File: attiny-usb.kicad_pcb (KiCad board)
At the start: 2 copper layers, 41.6 x 16.4 mm, 13 parts, among them J2 Conn_01x06, J3 Conn_01x02, U1 ATtiny85-20P

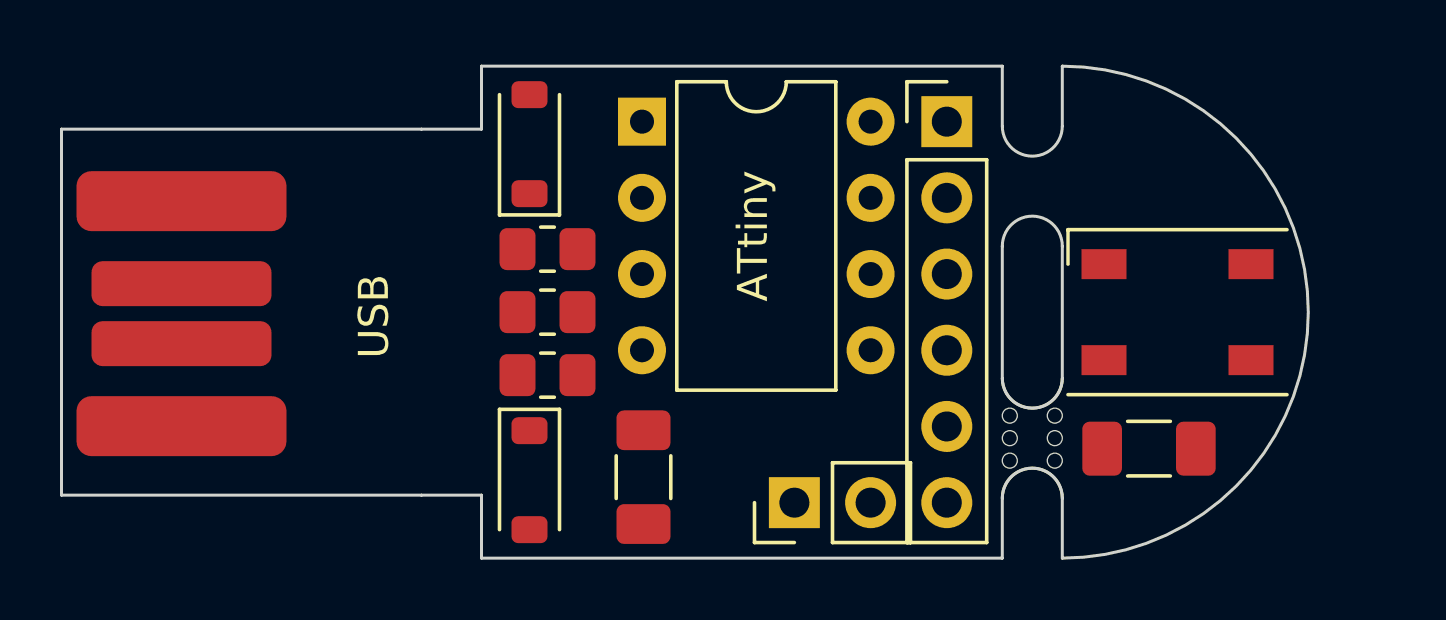
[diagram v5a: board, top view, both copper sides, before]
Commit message: route tracks. no errors
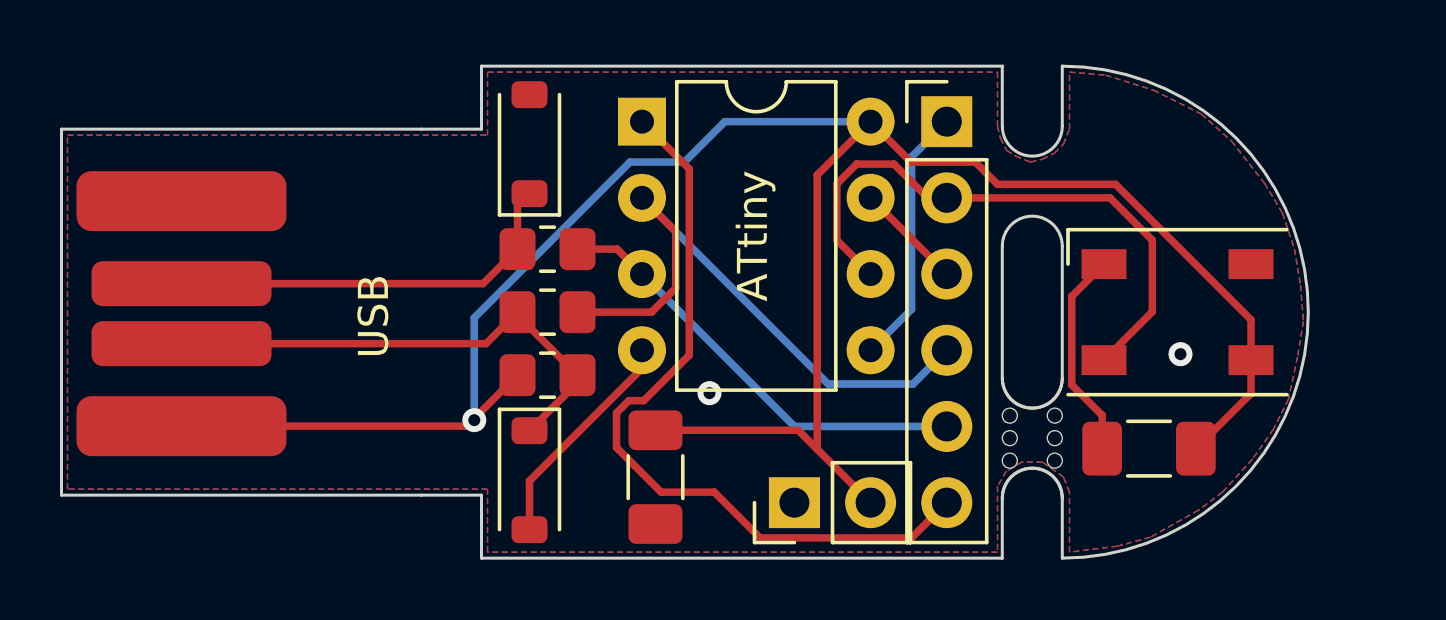
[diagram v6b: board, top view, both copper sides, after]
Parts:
- D3: value SK6812 -> WS2812B
- moved C1 0.40 mm to (119.8, 111.6)
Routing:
- net +5V: track 0.00 -> 71.6 mm, vias 0 -> 1
- net Net-(J2-Pin_6): track 0.00 -> 25.6 mm
- net Net-(J2-Pin_4): track 0.00 -> 20.3 mm
- net Net-(D3-DIN): track 0.00 -> 20.0 mm
- net Net-(D1-K): track 0.00 -> 17.1 mm
- net Net-(J2-Pin_5): track 0.00 -> 14.8 mm
- net GND: track 0.00 -> 14.5 mm, vias 0 -> 2
- net Net-(D2-K): track 0.00 -> 13.7 mm
- net Net-(J2-Pin_1): track 0.00 -> 8.67 mm
- net Net-(J2-Pin_3): track 0.00 -> 3.59 mm
- added copper zone on B.Cu, net GND
- added copper zone on F.Cu, net GND
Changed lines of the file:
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@@
   (setup
     (pad_to_mask_clearance 0)
-    (grid_origin 131.36 108.3)
     (pcbplotparams
       (layerselection 0x00010fc_ffffffff)
@@
   )
   (footprint "Capacitor_SMD:C_1206_3216Metric_Pad1.33x1.80mm_HandSolder" (layer "F.Cu")
-    (at 119.4 111.6 -90)
+    (at 119.8 111.6 -90)
     (descr "Capacitor SMD 1206 (3216 Metric), square (rectangular) end terminal, IPC_7351 nominal with elongated pad for handsoldering. (Body size source: IPC-SM-782 page 76, https://www.pcb-3d.com/wordpress/wp-content/uploads/ipc-sm-782a_amendment_1_and_2.pdf), generated with kicad-footprint-generator")
     (tags "capacitor handsolder")
@@
         (effects (font (size 1 1) (thickness 0.15)))
     )
-    (fp_text value "SK6812" (at 0.1 3.55) (layer "F.Fab")
+    (fp_text value "WS2812B" (at 0.1 3.55) (layer "F.Fab")
         (effects (font (size 1 1) (thickness 0.15)))
     )
@@
   (gr_line (start 131.36 97.9) (end 131.36 99.9)
     (stroke (width 0.1) (type default)) (layer "Edge.Cuts"))
+  (segment (start 125.19 110.67) (end 125.19 101.53) (width 0.25) (layer "F.Cu") (net 1))
+  (segment (start 128.32 101.1) (end 130.46 101.1) (width 0.25) (layer "F.Cu") (net 1))
+  (segment (start 135.136396 101.84) (end 139.65 106.353604) (width 0.25) (layer "F.Cu") (net 1))
+  (segment (start 126.97 99.75) (end 128.32 101.1) (width 0.25) (layer "F.Cu") (net 1))
+  (segment (start 139.65 106.353604) (end 139.65 107.7) (width 0.25) (layer "F.Cu") (net 1))
+  (segment (start 125.19 110.67) (end 126.97 112.45) (width 0.25) (layer "F.Cu") (net 1))
+  (segment (start 113.5 109.9) (end 113.7 109.7) (width 0.25) (layer "F.Cu") (net 1))
+  (segment (start 113.76 109.7) (end 113.76 109.64) (width 0.25) (layer "F.Cu") (net 1))
+  (segment (start 139.65 108.8125) (end 139.65 107.7) (width 0.25) (layer "F.Cu") (net 1))
+  (segment (start 130.46 101.1) (end 131.2 101.84) (width 0.25) (layer "F.Cu") (net 1))
+  (segment (start 124.5575 110.0375) (end 125.19 110.67) (width 0.25) (layer "F.Cu") (net 1))
+  (segment (start 113.76 109.64) (end 115.2 108.2) (width 0.25) (layer "F.Cu") (net 1))
+  (segment (start 119.8 110.0375) (end 124.5575 110.0375) (width 0.25) (layer "F.Cu") (net 1))
+  (segment (start 104 109.9) (end 113.5 109.9) (width 0.25) (layer "F.Cu") (net 1))
+  (segment (start 125.19 101.53) (end 126.97 99.75) (width 0.25) (layer "F.Cu") (net 1))
+  (segment (start 113.7 109.7) (end 113.76 109.7) (width 0.25) (layer "F.Cu") (net 1))
+  (segment (start 137.8125 110.65) (end 139.65 108.8125) (width 0.25) (layer "F.Cu") (net 1))
+  (segment (start 131.2 101.84) (end 135.136396 101.84) (width 0.25) (layer "F.Cu") (net 1))
+  (via (at 113.76 109.7) (size 0.8) (drill 0.4) (layers "F.Cu" "B.Cu") (net 1))
+  (segment (start 118.949009 101.1) (end 120.76 101.1) (width 0.25) (layer "B.Cu") (net 1))
+  (segment (start 122.11 99.75) (end 126.97 99.75) (width 0.25) (layer "B.Cu") (net 1))
+  (segment (start 120.76 101.1) (end 122.11 99.75) (width 0.25) (layer "B.Cu") (net 1))
+  (segment (start 113.76 106.289009) (end 118.949009 101.1) (width 0.25) (layer "B.Cu") (net 1))
+  (segment (start 113.76 109.7) (end 113.76 106.289009) (width 0.25) (layer "B.Cu") (net 1))
+  (segment (start 133.675 108.525) (end 133.675 105.575) (width 0.25) (layer "F.Cu") (net 2))
+  (segment (start 119.35 107.975431) (end 115.6 111.725431) (width 0.25) (layer "F.Cu") (net 2))
+  (segment (start 134.6875 110.65) (end 134.6875 109.5375) (width 0.25) (layer "F.Cu") (net 2))
+  (segment (start 134.6875 109.5375) (end 133.675 108.525) (width 0.25) (layer "F.Cu") (net 2))
+  (segment (start 119.35 107.37) (end 119.35 107.975431) (width 0.25) (layer "F.Cu") (net 2))
+  (segment (start 115.6 111.725431) (end 115.6 113.35) (width 0.25) (layer "F.Cu") (net 2))
+  (segment (start 133.675 105.575) (end 134.75 104.5) (width 0.25) (layer "F.Cu") (net 2))
+  (via (at 121.6 108.8) (size 0.8) (drill 0.4) (layers "F.Cu" "B.Cu") (free) (net 2))
+  (via (at 137.3 107.5) (size 0.8) (drill 0.4) (layers "F.Cu" "B.Cu") (free) (net 2))
+  (segment (start 115.2 106.1) (end 115.2 106.2) (width 0.25) (layer "F.Cu") (net 3))
+  (segment (start 114.15 107.15) (end 115.2 106.1) (width 0.25) (layer "F.Cu") (net 3))
+  (segment (start 117.2 108.45) (end 117.2 108.2) (width 0.25) (layer "F.Cu") (net 3))
+  (segment (start 104 107.15) (end 114.15 107.15) (width 0.25) (layer "F.Cu") (net 3))
+  (segment (start 115.2 106.2) (end 117.2 108.2) (width 0.25) (layer "F.Cu") (net 3))
+  (segment (start 115.6 110.05) (end 117.2 108.45) (width 0.25) (layer "F.Cu") (net 3))
+  (segment (start 115.2 104) (end 115.2 102.55) (width 0.25) (layer "F.Cu") (net 4))
+  (segment (start 104 105.15) (end 114.05 105.15) (width 0.25) (layer "F.Cu") (net 4))
+  (segment (start 115.2 102.55) (end 115.6 102.15) (width 0.25) (layer "F.Cu") (net 4))
+  (segment (start 114.05 105.15) (end 115.2 104) (width 0.25) (layer "F.Cu") (net 4))
+  (segment (start 128.873604 102.29) (end 129.51 102.29) (width 0.25) (layer "F.Cu") (net 5))
+  (segment (start 125.845 101.824009) (end 126.504009 101.165) (width 0.25) (layer "F.Cu") (net 5))
+  (segment (start 134.95 102.29) (end 136.36 103.7) (width 0.25) (layer "F.Cu") (net 5))
+  (segment (start 136.36 106.09) (end 134.75 107.7) (width 0.25) (layer "F.Cu") (net 5))
+  (segment (start 126.504009 101.165) (end 127.748604 101.165) (width 0.25) (layer "F.Cu") (net 5))
+  (segment (start 127.748604 101.165) (end 128.873604 102.29) (width 0.25) (layer "F.Cu") (net 5))
+  (segment (start 136.36 103.7) (end 136.36 106.09) (width 0.25) (layer "F.Cu") (net 5))
+  (segment (start 125.845 103.705) (end 125.845 101.824009) (width 0.25) (layer "F.Cu") (net 5))
+  (segment (start 126.97 104.83) (end 125.845 103.705) (width 0.25) (layer "F.Cu") (net 5))
+  (segment (start 129.51 102.29) (end 134.95 102.29) (width 0.25) (layer "F.Cu") (net 5))
+  (segment (start 126.97 107.37) (end 128.335 106.005) (width 0.25) (layer "B.Cu") (net 6))
+  (segment (start 128.335 100.925) (end 129.51 99.75) (width 0.25) (layer "B.Cu") (net 6))
+  (segment (start 128.335 106.005) (end 128.335 100.925) (width 0.25) (layer "B.Cu") (net 6))
+  (segment (start 126.97 102.29) (end 129.51 104.83) (width 0.25) (layer "F.Cu") (net 7))
+  (segment (start 119.670991 106.1) (end 120.475 105.295991) (width 0.25) (layer "F.Cu") (net 8))
+  (segment (start 120.475 103.415) (end 119.35 102.29) (width 0.25) (layer "F.Cu") (net 8))
+  (segment (start 120.475 105.295991) (end 120.475 103.415) (width 0.25) (layer "F.Cu") (net 8))
+  (segment (start 117.2 106.1) (end 119.670991 106.1) (width 0.25) (layer "F.Cu") (net 8))
+  (segment (start 119.35 102.29) (end 125.555 108.495) (width 0.25) (layer "B.Cu") (net 8))
+  (segment (start 128.385 108.495) (end 129.51 107.37) (width 0.25) (layer "B.Cu") (net 8))
+  (segment (start 125.555 108.495) (end 128.385 108.495) (width 0.25) (layer "B.Cu") (net 8))
+  (segment (start 118.52 104) (end 119.35 104.83) (width 0.25) (layer "F.Cu") (net 9))
+  (segment (start 117.2 104) (end 118.52 104) (width 0.25) (layer "F.Cu") (net 9))
+  (segment (start 124.43 109.91) (end 129.51 109.91) (width 0.25) (layer "B.Cu") (net 9))
+  (segment (start 119.35 104.83) (end 124.43 109.91) (width 0.25) (layer "B.Cu") (net 9))
+  (segment (start 119.41 109.05) (end 118.911827 109.05) (width 0.25) (layer "F.Cu") (net 11))
+  (segment (start 118.911827 109.05) (end 118.5 109.461827) (width 0.25) (layer "F.Cu") (net 11))
+  (segment (start 118.5 109.461827) (end 118.5 110.613173) (width 0.25) (layer "F.Cu") (net 11))
+  (segment (start 121.76 112.1) (end 123.285 113.625) (width 0.25) (layer "F.Cu") (net 11))
+  (segment (start 120.925 107.535) (end 119.41 109.05) (width 0.25) (layer "F.Cu") (net 11))
+  (segment (start 128.335 113.625) (end 129.51 112.45) (width 0.25) (layer "F.Cu") (net 11))
+  (segment (start 120.925 101.325) (end 120.925 107.535) (width 0.25) (layer "F.Cu") (net 11))
+  (segment (start 123.285 113.625) (end 128.335 113.625) (width 0.25) (layer "F.Cu") (net 11))
+  (segment (start 119.35 99.75) (end 120.925 101.325) (width 0.25) (layer "F.Cu") (net 11))
+  (segment (start 119.986827 112.1) (end 121.76 112.1) (width 0.25) (layer "F.Cu") (net 11))
+  (segment (start 118.5 110.613173) (end 119.986827 112.1) (width 0.25) (layer "F.Cu") (net 11))
+  (zone (net 2) (net_name "GND") (layers "F&B.Cu") (hatch edge 0.5)
+    (connect_pads (clearance 0.5))
+    (min_thickness 0.25) (filled_areas_thickness no)
+    (fill yes (thermal_gap 0.5) (thermal_bridge_width 0.5))
+    (polygon
+      (pts
+        (xy 100.2 100.2)
+        (xy 114.2 100.2)
+        (xy 114.2 98.1)
+        (xy 131.2 98.1)
+        (xy 131.2 99.9)
+        (xy 131.3 100.3)
+        (xy 131.5 100.7)
+        (xy 131.8 100.9)
+        (xy 132.3 101.1)
+        (xy 132.7 101)
+        (xy 133.1 100.8)
+        (xy 133.4 100.5)
+        (xy 133.6 100)
+        (xy 133.6 98.1)
+        (xy 134.8 98.2)
+        (xy 136.4 98.7)
+        (xy 138 99.5)
+        (xy 139 100.4)
+        (xy 140.1 101.8)
+        (xy 140.7 102.8)
+        (xy 141.1 104)
+        (xy 141.3 105.2)
+        (xy 141.4 106.4)
+        (xy 141.2 107.6)
+        (xy 140.9 109)
+        (xy 140.4 110)
+        (xy 139.7 111)
+        (xy 138.7 112.1)
+        (xy 137.9 112.7)
+        (xy 136.3 113.6)
+        (xy 135.2 113.9)
+        (xy 133.6 114.1)
+        (xy 133.6 112.1)
+        (xy 133.4 111.6)
+        (xy 132.7 111.1)
+        (xy 132 111.1)
+        (xy 131.5 111.4)
+        (xy 131.2 111.9)
+        (xy 131.2 114.1)
+        (xy 114.2 114.1)
+        (xy 114.2 112)
+        (xy 100.2 112)
+      )
+    )
+  )
 )

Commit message: correct footprint of C1,C2 and add header for Neopixel output
fixes #2
fixes #3
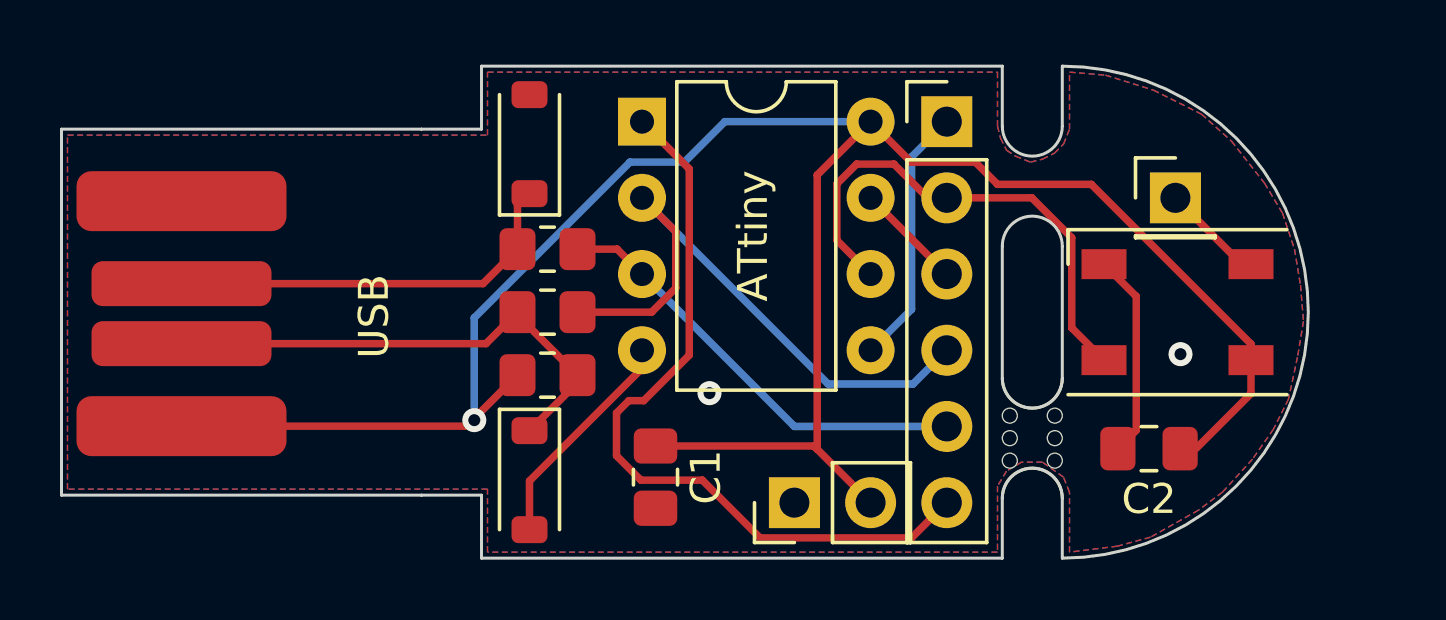
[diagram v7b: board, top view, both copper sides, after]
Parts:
- added J1: Conn_01x01, Connector_PinHeader_2.54mm:PinHeader_1x01_P2.54mm_Vertical, F.Cu at (137.1, 102.3)
- C1, C2: footprint Capacitor_SMD:C_1206_3216Metric_Pad1.33x1.80mm_HandSolder -> Capacitor_SMD:C_0805_2012Metric_Pad1.18x1.45mm_HandSolder
- D3: value WS2812B -> SK6812
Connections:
- D3 pad 4: unconnected-(D3-DOUT-Pad4) -> Net-(D3-DOUT)
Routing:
- net Net-(D3-DOUT): track 0.00 -> 3.44 mm
- net Net-(D3-DIN): track 20.0 -> 17.1 mm
- net +5V: track 71.6 -> 70.9 mm
